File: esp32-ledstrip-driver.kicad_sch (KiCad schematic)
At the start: 43 parts, among them P1 PWR, P2 LED_1, P3 LED_2, P4 LED_3, P5 LED_4, P6 RS485, Q1 FDD8880?, Q2 FDD8880?, Q3 FDD8880?, Q4 FDD8880?, Q5 FDD8880?, Q6 FDD8880?, Q7 FDD8880?, Q8 FDD8880?, U1 ESP32-WROOM-32, U2 R-78E-1.0, U3 MAX481E

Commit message: first gerbers generated
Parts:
- added D6: Led_Small, LED_SMD:LED_0805_2012Metric_Pad1.15x1.40mm_HandSolder, symbol wazombi:Led_Small
- added R26: 220R, Resistor_SMD:R_0603_1608Metric, symbol wazombi:R_Small
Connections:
- net DI: now also U1.12 (IO27)
- net GND: now also R26.1
- net RO: now also U1.11 (IO26)
- net ~{RX}TX: now also U1.8 (IO32)
- net at R17.2, R19.2: now also P6.3 (P3); no longer P6.1 (P1)
- net GPIO_2: now reaches U1.24 (IO2)
- net GPIO_0: now reaches U1.25 (IO0)
- net at U1.29 (IO5): now also D6.2 (A)
- net ESP_EN: now reaches U1.3 (EN)
- net RXD_0: now reaches U1.34 (RXD0/IO3)
- net TXD_0: now reaches U1.35 (TXD0/IO1)
- net at R18.2, R19.1: now also P6.1 (P1); no longer P6.3 (P3)
- new net: D6.1 (K), R26.2
- no-connect marks 6 -> 8
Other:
- added sheet esp-usb-prog (esp-usb-prog.kicad_sch)
- moved on the sheet: C1, C2, L1, U2

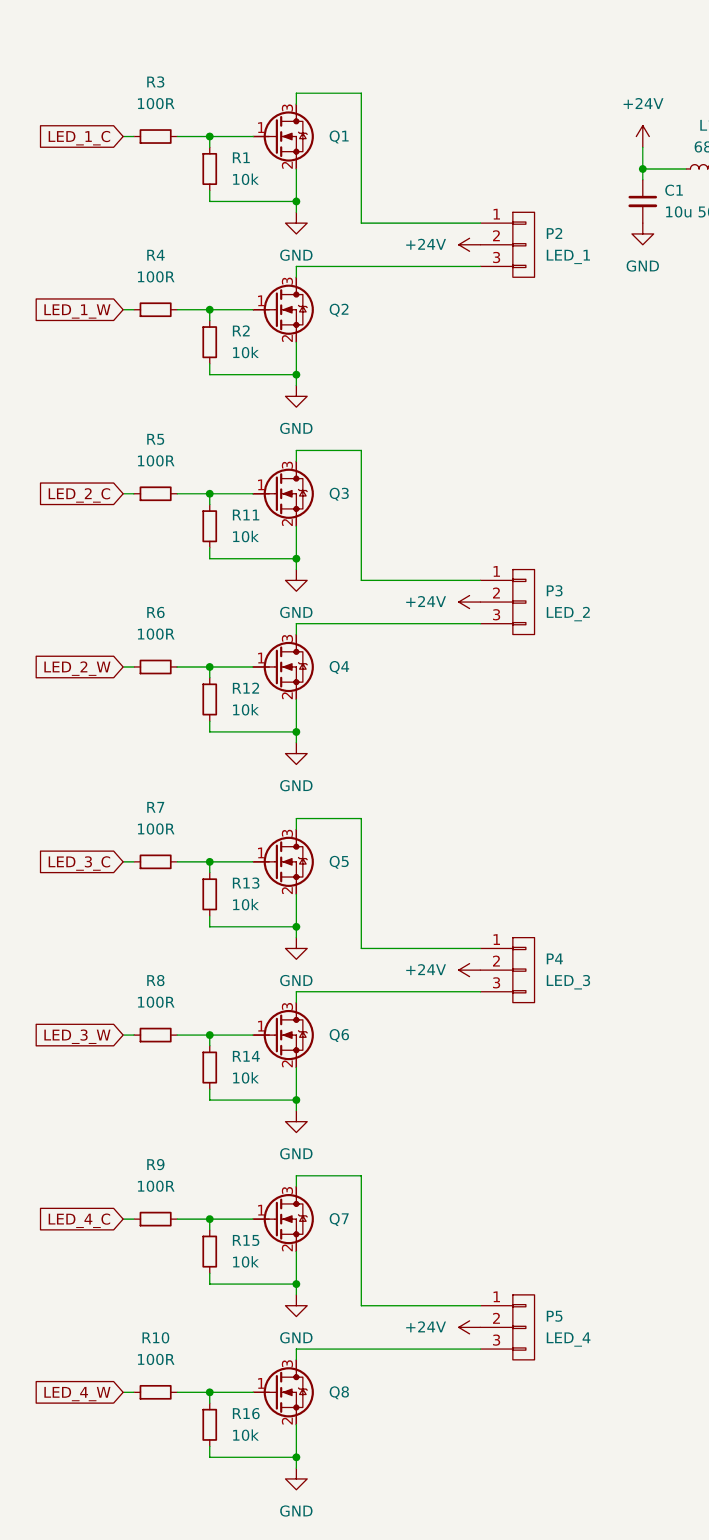
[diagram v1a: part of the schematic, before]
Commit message: Fixed FET footprints
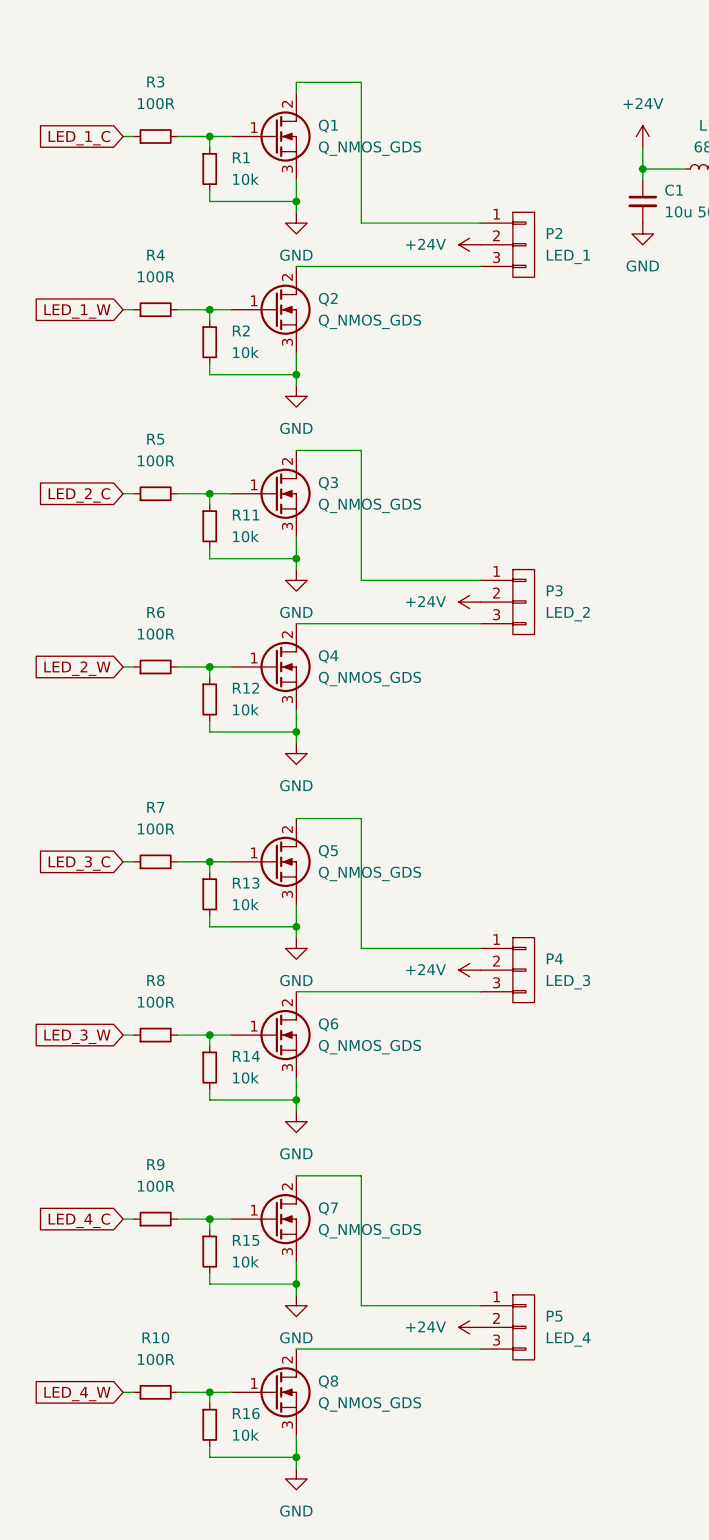
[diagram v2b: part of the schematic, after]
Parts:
- removed Q1, Q2, Q3, Q4, Q5, Q6, Q7, Q8: FDD8880?, Package_TO_SOT_SMD:TO-252-2, symbol wazombi:Q_NMOS_GSD_SMALL
- added Q1, Q2, Q3, Q4, Q5, Q6, Q7, Q8: Q_NMOS_GDS, Package_TO_SOT_SMD:TO-252-2, symbol Wazombi:Q_NMOS_GDS
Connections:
- net GND: now also Q1.3 (S), Q2.3 (S), Q3.3 (S), Q4.3 (S), Q5.3 (S), Q6.3 (S), Q7.3 (S), Q8.3 (S)
- net at R12.1, R6.2: now also Q4.1 (G)
- net at P4.1 (P1): now also Q5.2 (D)
- net at P4.3 (P3): now also Q6.2 (D)
- net at R10.2, R16.1: now also Q8.1 (G)
- net at R15.1, R9.2: now also Q7.1 (G)
- net at R2.1, R4.2: now also Q2.1 (G)
- net at R1.1, R3.2: now also Q1.1 (G)
- net at P5.1 (P1): now also Q7.2 (D)
- net at R13.1, R7.2: now also Q5.1 (G)
- net at P3.3 (P3): now also Q4.2 (D)
- net at R11.1, R5.2: now also Q3.1 (G)
- net at P3.1 (P1): now also Q3.2 (D)
- net at R14.1, R8.2: now also Q6.1 (G)
- net at P2.1 (P1): now also Q1.2 (D)
- net at P2.3 (P3): now also Q2.2 (D)
- net at P5.3 (P3): now also Q8.2 (D)

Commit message: WIP
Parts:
- removed Q3, Q4, Q5, Q6, Q7, Q8: Q_NMOS_GDS, Package_TO_SOT_SMD:TO-252-2, symbol Wazombi:Q_NMOS_GDS
- removed R10, R3, R4, R5, R6, R7, R8, R9: 100R, Resistor_SMD:R_0603_1608Metric, symbol wazombi:R_Small
- removed R11, R12, R13, R14, R15, R16: 10k, Resistor_SMD:R_0603_1608Metric, symbol wazombi:R_Small
- added C10: 10u 50V, Capacitor_SMD:C_1210_3225Metric, symbol wazombi:C_Small
- added C11: 220u, Capacitor_THT:CP_Radial_D8.0mm_P3.50mm, symbol Wazombi:CP_Small
- added C9: 100n, Capacitor_SMD:C_0603_1608Metric, symbol wazombi:C_Small
- added D7: D_Schottky_Small, Diode_SMD:D_SMA, symbol wazombi:D_Schottky_Small
- added J2: 1-Wire, TerminalBlock:TerminalBlock_bornier-3_P5.08mm, symbol Connector_Generic:Conn_01x03
- added J3: Conn_01x08, Connector_PinHeader_2.54mm:PinHeader_1x08_P2.54mm_Vertical, symbol Connector_Generic:Conn_01x08
- added J4: Conn_01x08, TerminalBlock_Phoenix:TerminalBlock_Phoenix_MKDS-1,5-8-5.08_1x08_P5.08mm_Horizontal, symbol Connector_Generic:Conn_01x08
- added L2: 68u, Inductor_SMD:L_6.3x6.3_H3, symbol wazombi:L_Small
- added L3: 330uH, Inductor_SMD:L_6.3x6.3_H3, symbol wazombi:L_Small
- added Q11, Q12, Q3, Q4, Q5, Q6, Q7, Q8: Q_NMOS_GSD_SMALL, Package_TO_SOT_SMD:SOT-23, symbol Wazombi:Q_NMOS_GSD_SMALL
- added Q13, Q14, Q15, Q16, Q17, Q18: Q_NMOS_GDS, Package_TO_SOT_SMD:TO-252-2, symbol Wazombi:Q_NMOS_GDS
- added R10, R3, R34, R35, R36, R37, R38, R39, R4, R40, R41, R5, R6, R7, R8, R9: 100R, Resistor_SMD:R_0402_1005Metric, symbol Wazombi:R_Small
- added R11, R12, R13, R14, R15, R16, R32, R33: 10k, Resistor_SMD:R_0402_1005Metric, symbol Wazombi:R_Small
- added R28, R50, R51, R52, R53, R54, R55: 10k, Resistor_SMD:R_0603_1608Metric, symbol wazombi:R_Small
- added R29, R30, R31: 4k7, Resistor_SMD:R_0603_1608Metric, symbol wazombi:R_Small
- added R42, R43, R44, R45, R46, R47, R48, R49: 1k, Resistor_SMD:R_0402_1005Metric, symbol Wazombi:R_Small
- added R56: 1k, Resistor_SMD:R_0603_1608Metric, symbol wazombi:R_Small
- added R57: 7k15, Resistor_SMD:R_0603_1608Metric, symbol wazombi:R_Small
- added U10, U11, U12, U13, U6, U7, U8, U9: ZXGD3009E6, Package_TO_SOT_SMD:SOT-23-6, symbol Driver_FET:ZXGD3009E6
- added U14: LM2574M-ADJ, Package_SO:SOIC-14W_7.5x9mm_P1.27mm, symbol Regulator_Switching:LM2574M-ADJ
- added U5: PCF8575, Package_SO:SSOP-24_5.3x8.2mm_P0.65mm, symbol Wazombi:PCF8575
- P4: value LED_3 -> LED_4
- P5: value LED_4 -> LED_3
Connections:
- net +24V: now also L2.1
- net +3V3: now also C9.1, J2.2 (Pin_2), R28.1, R29.2, R30.2, R31.2, U5.24 (VDD)
- net GND: now also C10.1, C11.2, C9.2, D7.2 (A), J2.3 (Pin_3), J3.2 (Pin_2), J3.4 (Pin_4), J3.6 (Pin_6), J3.8 (Pin_8), J4.2 (Pin_2), J4.4 (Pin_4), J4.6 (Pin_6), J4.8 (Pin_8), Q11.2 (S), Q12.2 (S), Q13.3 (S), Q14.3 (S), Q15.3 (S), Q16.3 (S), Q17.3 (S), Q18.3 (S), Q3.2 (S), Q4.2 (S), Q5.2 (S), Q6.2 (S), Q7.2 (S), Q8.2 (S), R11.1, R12.1, R13.1, R14.1, R15.1, R16.1, R32.1, R33.1, R50.2, R51.2, R52.2, R53.2, R54.2, R55.2, R56.1, U10.3 (VEE), U11.3 (VEE), U12.3 (VEE), U13.3 (VEE), U14.4 (SGND), U14.5 (~{ON}/OFF), U14.6 (PGND), U5.12 (GND), U5.2 (A1), U5.21 (A0), U5.3 (A2), U6.3 (VEE), U7.3 (VEE), U8.3 (VEE), U9.3 (VEE)
- net LED_1_C: now also R3.1
- net LED_1_W: now also R4.1
- net LED_2_C: now also R5.1
- net LED_2_W: now also R6.1
- net LED_3_C: now also U1.9 (IO33), R9.1; no longer U1.33 (IO21)
- net LED_3_W: now also U1.16 (IO13), R10.1; no longer U1.36 (IO22)
- net LED_4_C: now also R7.1
- net LED_4_W: now also R8.1
- net at Q1.1 (G), R1.1: now also U6.4 (SINK), U6.6 (SOURCE)
- net at P4.1 (P1): now also Q15.2 (D)
- net at P4.3 (P3): now also Q16.2 (D)
- net at Q2.1 (G), R2.1: now also U7.4 (SINK), U7.6 (SOURCE)
- net at D6.2 (A): now also U1.23 (IO15); no longer U1.29 (IO5)
- net 1-WIRE: now reaches U1.26 (IO4)
- net 1-WIRE: now also J2.1 (Pin_1), R30.1
- net ~{IO_INT}: now reaches U1.6 (IO34)
- net ~{IO_INT}: now also R28.2, U5.1 (~{INT})
- net at P3.3 (P3): now also Q14.2 (D)
- net at P3.1 (P1): now also Q13.2 (D)
- net at P5.1 (P1): now also Q17.2 (D)
- net at P5.3 (P3): now also Q18.2 (D)
- new net: R56.2, R57.1, U14.3 (FB)
- new net: Q16.1 (G), R53.1, U11.4 (SINK), U11.6 (SOURCE)
- new net: Q5.3 (D), R36.1
- new net: R36.2, R44.2, U8.2 (IN)
- new net: Q14.1 (G), R51.1, U9.4 (SINK), U9.6 (SOURCE)
- new net: D7.1 (K), L3.1, U14.12 (OUT)
- new net: R37.2, R45.2, U9.2 (IN)
- new net: R39.2, R47.2, U11.2 (IN)
- new net: Q7.1 (G), R15.2, R7.2
- new net: Q7.3 (D), R38.1
- new net: Q8.1 (G), R16.2, R8.2
- new net: Q6.1 (G), R14.2, R6.2
- new net: R34.2, R42.2, U6.2 (IN)
- new net: Q15.1 (G), R52.1, U10.4 (SINK), U10.6 (SOURCE)
- new net: R38.2, R46.2, U10.2 (IN)
- new net: Q4.1 (G), R12.2, R4.2
- new net: Q3.1 (G), R11.2, R3.2
- new net: Q3.3 (D), R34.1
- new net: J4.1 (Pin_1), U5.16 (P13)
- new net: J4.3 (Pin_3), U5.15 (P12)
- new net: J4.5 (Pin_5), U5.14 (P11)
- new net: J4.7 (Pin_7), U5.13 (P10)
- new net: Q4.3 (D), R35.1
- new net: C10.2, L2.2, U14.10 (VIN)
- new net: Q17.1 (G), R54.1, U12.4 (SINK), U12.6 (SOURCE)
- new net: Q12.1 (G), R10.2, R33.2
- new net: Q5.1 (G), R13.2, R5.2
- new net: Q18.1 (G), R55.1, U13.4 (SINK), U13.6 (SOURCE)
- new net: Q11.1 (G), R32.2, R9.2
- new net: Q11.3 (D), R40.1
- new net: R35.2, R43.2, U7.2 (IN)
- new net: J3.1 (Pin_1), U5.20 (P17)
- new net: J3.3 (Pin_3), U5.19 (P16)
- new net: J3.5 (Pin_5), U5.18 (P15)
- new net: J3.7 (Pin_7), U5.17 (P14)
- new net: R41.2, R49.2, U13.2 (IN)
- new net: R40.2, R48.2, U12.2 (IN)
- new net: Q6.3 (D), R37.1
- new net: Q13.1 (G), R50.1, U8.4 (SINK), U8.6 (SOURCE)
- new net: Q12.3 (D), R41.1
- new net: Q8.3 (D), R39.1
- new net +10V: C11.1, L3.2, R42.1, R43.1, R44.1, R45.1, R46.1, R47.1, R48.1, R49.1, R57.2, U10.1 (VCC), U11.1 (VCC), U12.1 (VCC), U13.1 (VCC), U6.1 (VCC), U7.1 (VCC), U8.1 (VCC), U9.1 (VCC)
- new net SCL: R29.1, U1.36 (IO22), U5.22 (SCL)
- new net SDA: R31.1, U1.33 (IO21), U5.23 (SDA)
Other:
- note added: "1. Ukse asendi andur 2. Uksekella nupp 3. 1-wire 4. Luku andur? 5. Lüliti 6. Liikumisandur"
- moved on the sheet: C1, C2, D1, D6, F1, L1, P1, P2, Q1, Q2, R1, R2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
